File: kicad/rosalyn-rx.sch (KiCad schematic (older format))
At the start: 36 parts, among them J2 Serial1, J3 Serial2, J4 PWM, U1 STM32F303CCTx, U2 E22-EBYTE, U3 XC6206P330MR, U4 TXS0108EPW, U5 BMP280, U6 ICM-20602

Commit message: updated nvdata driver
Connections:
- net e22_busy renamed radio_busy
- net e22_dio1 renamed radio_dio1
- net e22_dio2 renamed radio_dio2
- net e22_nrst renamed radio_nrst
- net e22_nss renamed radio_nss
- net e22_rxen renamed radio_rxen
- net e22_txen renamed radio_txen
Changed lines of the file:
@@
 Sheet 1 1
 Title "RosalynRX"
-Date "2020-11-17"
+Date "2020-11-23"
 Rev "v1.0"
 Comp "www.2-0.dk"
@@
 NoConn ~ 6000 3100
 Text GLabel 6000 2650 0    50   Input ~ 0
-e22_nss
+radio_nss
 Text GLabel 6000 2750 0    50   Input ~ 0
 spi2_sck
@@
 spi2_mosi
 Text GLabel 7400 2650 2    50   Input ~ 0
-e22_rxen
+radio_rxen
 Text GLabel 7400 2750 2    50   Input ~ 0
-e22_txen
+radio_txen
 Text GLabel 7400 2850 2    50   BiDi ~ 0
-e22_dio1
+radio_dio1
 Text GLabel 7400 2950 2    50   BiDi ~ 0
-e22_dio2
+radio_dio2
 Text GLabel 7400 3050 2    50   Output ~ 0
-e22_busy
+radio_busy
 Text GLabel 7400 3150 2    50   Input ~ 0
-e22_nrst
+radio_nrst
 Text GLabel 3950 4500 2    50   Output ~ 0
 spi1_sck
@@
 spi2_mosi
 Text GLabel 2650 5200 0    50   Input ~ 0
-e22_nss
+radio_nss
 Text GLabel 3950 4800 2    50   Input ~ 0
-e22_nrst
+radio_nrst
 Text GLabel 3950 4900 2    50   Output ~ 0
-e22_busy
+radio_busy
 Text GLabel 3950 5000 2    50   BiDi ~ 0
-e22_dio1
+radio_dio1
 Text GLabel 2650 3600 0    50   BiDi ~ 0
-e22_dio2
+radio_dio2
 Text GLabel 2650 3700 0    50   Input ~ 0
-e22_txen
+radio_txen
 Text GLabel 2650 3800 0    50   Input ~ 0
-e22_rxen
+radio_rxen
 Text GLabel 9250 4550 0    50   Input ~ 0
 icm_nss

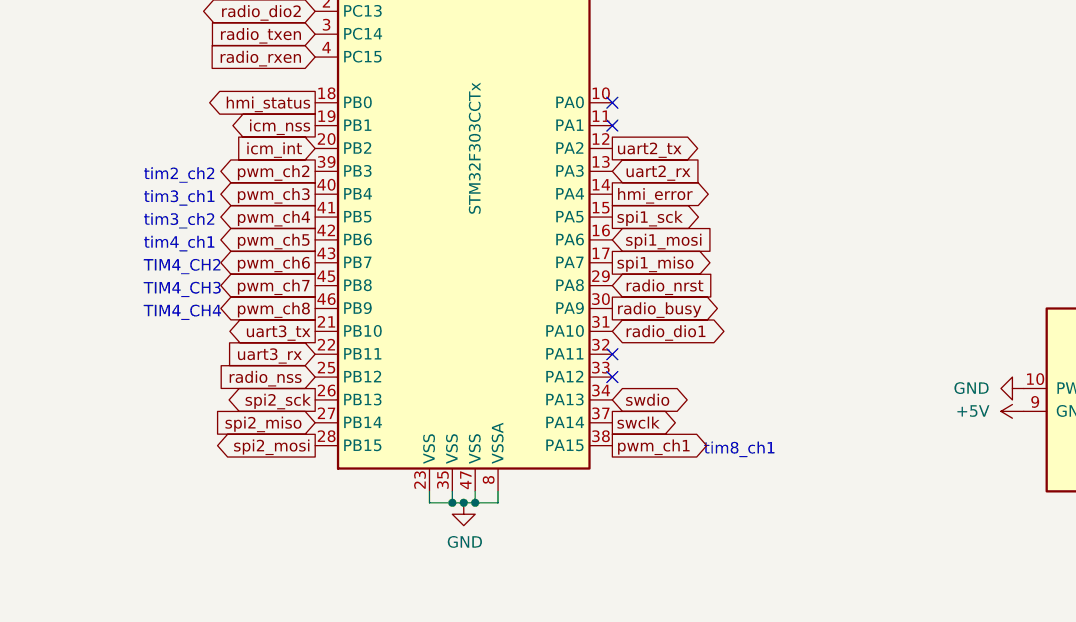
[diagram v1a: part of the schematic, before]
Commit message: added pwm support for ch1 to ch4
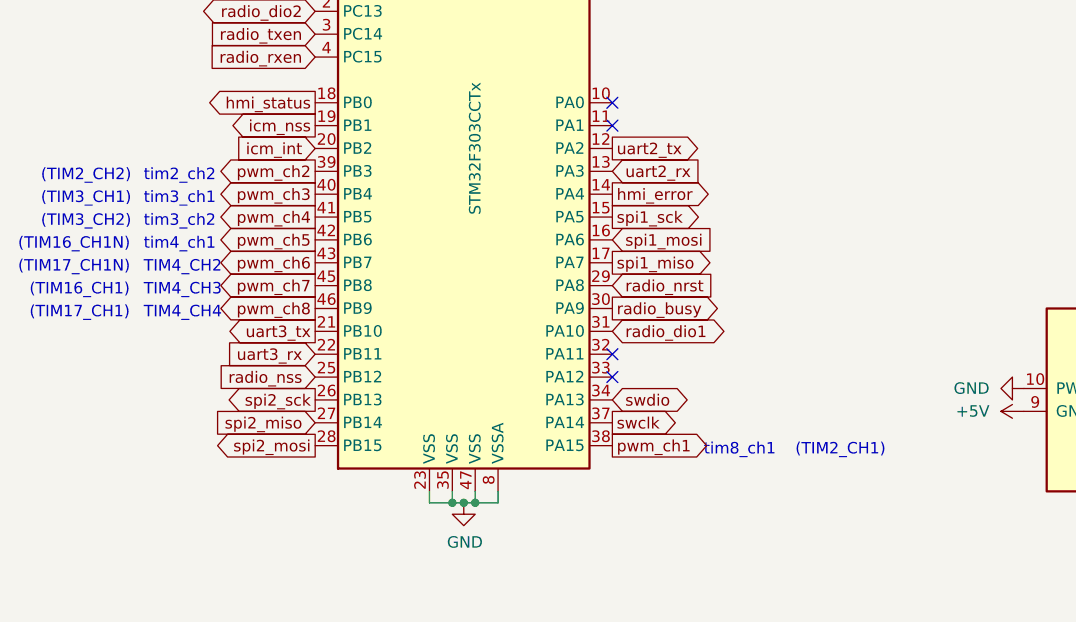
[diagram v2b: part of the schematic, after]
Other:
- note added: "(TIM16_CH1)"
- note added: "(TIM16_CH1N)"
- note added: "(TIM17_CH1)"
- note added: "(TIM17_CH1N)"
- note added: "(TIM2_CH1)"
- note added: "(TIM2_CH2)"
- note added: "(TIM3_CH1)"
- note added: "(TIM3_CH2)"
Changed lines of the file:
@@
 	1    0    0    -1
 $EndComp
+Text Notes 4750 5550 0    50   ~ 0
+(TIM2_CH1)
+Text Notes 1450 4350 0    50   ~ 0
+(TIM2_CH2)
+Text Notes 1450 4450 0    50   ~ 0
+(TIM3_CH1)
+Text Notes 1450 4550 0    50   ~ 0
+(TIM3_CH2)
+Text Notes 1400 4850 0    50   ~ 0
+(TIM16_CH1)
+Text Notes 1400 4950 0    50   ~ 0
+(TIM17_CH1)
+Text Notes 1350 4650 0    50   ~ 0
+(TIM16_CH1N)
+Text Notes 1350 4750 0    50   ~ 0
+(TIM17_CH1N)
 $EndSCHEMATC
